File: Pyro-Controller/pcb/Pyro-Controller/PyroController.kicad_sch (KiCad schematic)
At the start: 8 parts, among them Q1 SiS454DN

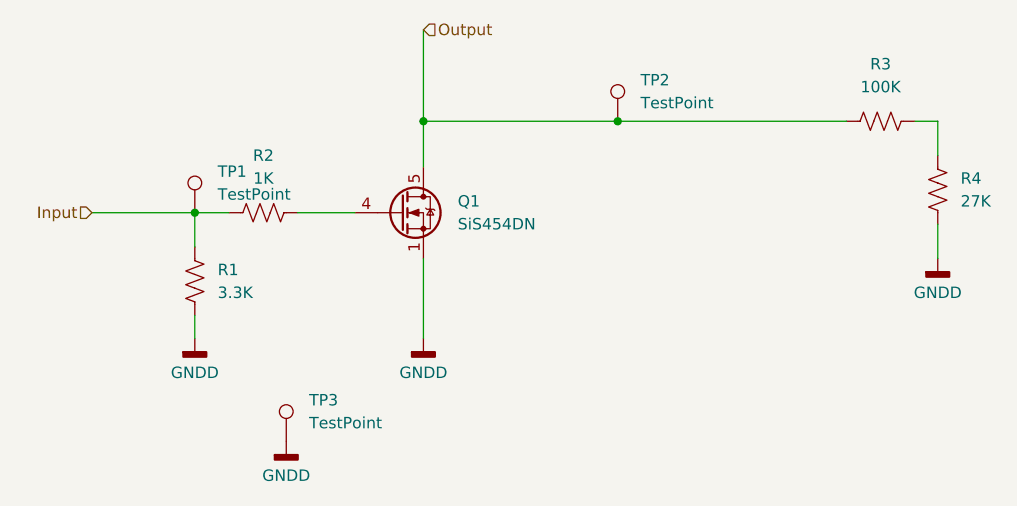
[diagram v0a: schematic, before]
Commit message: BOM, BOM Template, Rowan Rocketry Logo
- Finished pyro controller BOM
- Created template for BOMs
- Created a footprint for adding the Rowan Rocketry logo to PCBs
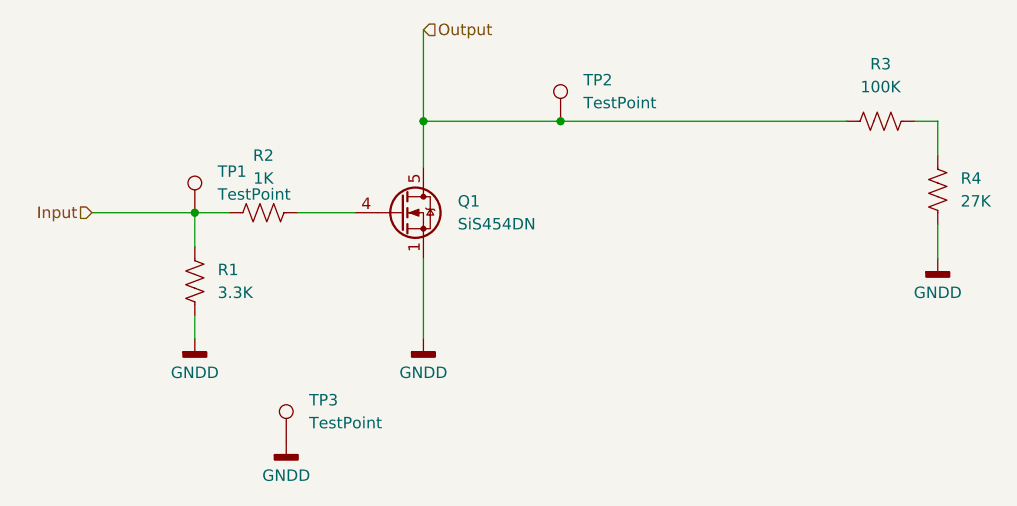
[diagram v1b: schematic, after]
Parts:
- Q1: Purchase (none) -> https://www.digikey.com/en/products/detail/vishay-siliconix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
- R1, R2, R4: Purchase (none) -> https://www.digikey.com/en/products/detail/yageo/RC0603JR-0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
- R3: Purchase (none) -> https://www.digikey.com/en/products/detail/yageo/RC0603JR-1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
- TP1, TP2, TP3: Purchase (none) -> https://www.digikey.com/en/products/detail/keystone-electro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
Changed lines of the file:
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@@
 	)
 	(junction
-		(at 137.16 77.47)
+		(at 130.81 77.47)
 		(diameter 0)
 		(color 0 0 0 0)
@@
 	(wire
 		(pts
-			(xy 137.16 77.47) (xy 162.56 77.47)
-		)
-		(stroke
-			(width 0)
-			(type default)
-		)
-	)
-	(wire
-		(pts
-			(xy 115.57 77.47) (xy 137.16 77.47)
+			(xy 115.57 77.47) (xy 130.81 77.47)
 		)
 		(stroke
@@
 		(pts
 			(xy 101.6 87.63) (xy 107.95 87.63)
+		)
+		(stroke
+			(width 0)
+			(type default)
+		)
+	)
+	(wire
+		(pts
+			(xy 130.81 77.47) (xy 162.56 77.47)
 		)
 		(stroke
@@
 			)
 		)
-		(property "Datasheet" "~"
+		(property "Datasheet" "https://www.yageo.com/upload/media/product/products/datasheet/rchip/PYu-RC_Group_51_RoHS_L_12.pdf"
 			(at 90.17 95.25 0)
 			(effects
@@
 			)
 		)
-		(property "MPN" ""
-			(at 90.17 95.25 0)
-			(effects
-				(font
-					(size 1.27 1.27)
-				)
-				(hide yes)
-			)
-		)
-		(property "Retailer" ""
+		(property "Purchase" "https://www.digikey.com/en/products/detail/yageo/RC0603JR-073K3L/726757?_gl=1*oprbzy*_up*MQ..&gclid=Cj0KCQjwj4K5BhDYARIsAD1Ly2qquIi0HITcnSJzEILMOtvyCB9wPLUQOH5qAcVxd7LGVxbBaQts_tIaAkVREALw_wcB"
 			(at 90.17 95.25 0)
 			(effects
@@
 			)
 		)
-		(property "Datasheet" "~"
+		(property "Datasheet" "https://www.yageo.com/upload/media/product/products/datasheet/rchip/PYu-RC_Group_51_RoHS_L_12.pdf"
 			(at 172.72 85.09 0)
 			(effects
@@
 			)
 		)
-		(property "MPN" ""
-			(at 172.72 85.09 0)
-			(effects
-				(font
-					(size 1.27 1.27)
-				)
-				(hide yes)
-			)
-		)
-		(property "Retailer" ""
+		(property "Purchase" "https://www.digikey.com/en/products/detail/yageo/RC0603JR-0727KL/726752"
 			(at 172.72 85.09 0)
 			(effects
@@
 			)
 		)
-		(property "Datasheet" "~"
+		(property "Datasheet" "https://www.yageo.com/upload/media/product/products/datasheet/rchip/PYu-RC_Group_51_RoHS_L_12.pdf"
 			(at 97.79 87.63 0)
 			(effects
@@
 			)
 		)
-		(property "MPN" ""
-			(at 97.79 87.63 0)
-			(effects
-				(font
-					(size 1.27 1.27)
-				)
-				(hide yes)
-			)
-		)
-		(property "Retailer" ""
+		(property "Purchase" "https://www.digikey.com/en/products/detail/yageo/RC0603JR-071KL/726677?_gl=1*1an2o6r*_up*MQ..&gclid=Cj0KCQjwj4K5BhDYARIsAD1Ly2qquIi0HITcnSJzEILMOtvyCB9wPLUQOH5qAcVxd7LGVxbBaQts_tIaAkVREALw_wcB"
 			(at 97.79 87.63 0)
 			(effects
@@
 	)
 	(symbol
+		(lib_id "Connector:TestPoint")
+		(at 130.81 77.47 0)
+		(unit 1)
+		(exclude_from_sim no)
+		(in_bom yes)
+		(on_board yes)
+		(dnp no)
+		(fields_autoplaced yes)
+		(property "Reference" "TP2"
+			(at 133.35 72.8979 0)
+			(effects
+				(font
+					(size 1.27 1.27)
+				)
+				(justify left)
+			)
+		)
+		(property "Value" "TestPoint"
+			(at 133.35 75.4379 0)
+			(effects
+				(font
+					(size 1.27 1.27)
+				)
+				(justify left)
+			)
+		)
+		(property "Footprint" "TestPoint:TestPoint_Loop_D2.54mm_Drill1.5mm_Beaded"
+			(at 135.89 77.47 0)
+			(effects
+				(font
+					(size 1.27 1.27)
+				)
+				(hide yes)
+			)
+		)
+		(property "Datasheet" "https://www.keyelco.com/userAssets/file/M65p56.pdf"
+			(at 135.89 77.47 0)
+			(effects
+				(font
+					(size 1.27 1.27)
+				)
+				(hide yes)
+			)
+		)
+		(property "Description" "test point"
+			(at 130.81 77.47 0)
+			(effects
+				(font
+					(size 1.27 1.27)
+				)
+				(hide yes)
+			)
+		)
+		(property "Purchase" "https://www.digikey.com/en/products/detail/keystone-electronics/5000/255326"
+			(at 130.81 77.47 0)
+			(effects
+				(font
+					(size 1.27 1.27)
+				)
+				(hide yes)
+			)
+		)
+		(pin "1"
+		)
+		(instances
+			(project "Pyro-Controller"
+				(path "/3d6591d1-15d3-4f90-b463-ad4ce370627d/d3fae8d6-dc5c-4ad1-8056-ef8170011280"
+					(reference "TP2")
+					(unit 1)
+				)
+			)
+		)
+	)
+	(symbol
 		(lib_id "Device:R_US")
 		(at 166.37 77.47 90)
@@
 			)
 		)
-		(property "Datasheet" "~"
+		(property "Datasheet" "https://www.yageo.com/upload/media/product/products/datasheet/rchip/PYu-RC_Group_51_RoHS_L_12.pdf"
 			(at 166.37 77.47 0)
 			(effects
@@
 			)
 		)
-		(property "MPN" ""
-			(at 166.37 77.47 0)
-			(effects
-				(font
-					(size 1.27 1.27)
-				)
-				(hide yes)
-			)
-		)
-		(property "Retailer" ""
+		(property "Purchase" "https://www.digikey.com/en/products/detail/yageo/RC0603JR-13100KL/13694230?_gl=1*1eq4xmo*_up*MQ..&gclid=Cj0KCQjwj4K5BhDYARIsAD1Ly2qquIi0HITcnSJzEILMOtvyCB9wPLUQOH5qAcVxd7LGVxbBaQts_tIaAkVREALw_wcB"
 			(at 166.37 77.47 0)
 			(effects
@@
 	(symbol
 		(lib_id "Connector:TestPoint")
-		(at 137.16 77.47 0)
-		(unit 1)
-		(exclude_from_sim no)
-		(in_bom yes)
-		(on_board yes)
-		(dnp no)
-		(fields_autoplaced yes)
-		(property "Reference" "TP2"
-			(at 139.7 72.8979 0)
+		(at 100.33 113.03 0)
+		(unit 1)
+		(exclude_from_sim no)
+		(in_bom yes)
+		(on_board yes)
+		(dnp no)
+		(fields_autoplaced yes)
+		(property "Reference" "TP3"
+			(at 102.87 108.4579 0)
 			(effects
 				(font
@@
 		)
 		(property "Value" "TestPoint"
-			(at 139.7 75.4379 0)
+			(at 102.87 110.9979 0)
 			(effects
 				(font
@@
 		)
 		(property "Footprint" "TestPoint:TestPoint_Loop_D2.54mm_Drill1.5mm_Beaded"
-			(at 142.24 77.47 0)
-			(effects
-				(font
-					(size 1.27 1.27)
-				)
-				(hide yes)
-			)
-		)
-		(property "Datasheet" "~"
-			(at 142.24 77.47 0)
+			(at 105.41 113.03 0)
+			(effects
+				(font
+					(size 1.27 1.27)
+				)
+				(hide yes)
+			)
+		)
+		(property "Datasheet" "https://www.keyelco.com/userAssets/file/M65p56.pdf"
+			(at 105.41 113.03 0)
 			(effects
 				(font
@@
 		)
 		(property "Description" "test point"
-			(at 137.16 77.47 0)
-			(effects
-				(font
-					(size 1.27 1.27)
-				)
-				(hide yes)
-			)
-		)
-		(property "MPN" ""
-			(at 137.16 77.47 0)
-			(effects
-				(font
-					(size 1.27 1.27)
-				)
-				(hide yes)
-			)
-		)
-		(property "Retailer" ""
-			(at 137.16 77.47 0)
+			(at 100.33 113.03 0)
+			(effects
+				(font
+					(size 1.27 1.27)
+				)
+				(hide yes)
+			)
+		)
+		(property "Purchase" "https://www.digikey.com/en/products/detail/keystone-electronics/5000/255326"
+			(at 100.33 113.03 0)
 			(effects
 				(font
@@
 			(project "Pyro-Controller"
 				(path "/3d6591d1-15d3-4f90-b463-ad4ce370627d/d3fae8d6-dc5c-4ad1-8056-ef8170011280"
-					(reference "TP2")
+					(reference "TP3")
 					(unit 1)
 				)
@@
 			)
 		)
-		(property "Datasheet" "~"
+		(property "Datasheet" "https://www.keyelco.com/userAssets/file/M65p56.pdf"
 			(at 95.25 87.63 0)
 			(effects
@@
 			)
 		)
-		(property "MPN" ""
-			(at 90.17 87.63 0)
-			(effects
-				(font
-					(size 1.27 1.27)
-				)
-				(hide yes)
-			)
-		)
-		(property "Retailer" ""
+		(property "Purchase" "https://www.digikey.com/en/products/detail/keystone-electronics/5000/255326"
 			(at 90.17 87.63 0)
 			(effects
@@
 	)
 	(symbol
-		(lib_id "Connector:TestPoint")
-		(at 100.33 113.03 0)
-		(unit 1)
-		(exclude_from_sim no)
-		(in_bom yes)
-		(on_board yes)
-		(dnp no)
-		(fields_autoplaced yes)
-		(property "Reference" "TP3"
-			(at 102.87 108.4579 0)
-			(effects
-				(font
-					(size 1.27 1.27)
-				)
-				(justify left)
-			)
-		)
-		(property "Value" "TestPoint"
-			(at 102.87 110.9979 0)
-			(effects
-				(font
-					(size 1.27 1.27)
-				)
-				(justify left)
-			)
-		)
-		(property "Footprint" "TestPoint:TestPoint_Loop_D2.54mm_Drill1.5mm_Beaded"
-			(at 105.41 113.03 0)
-			(effects
-				(font
-					(size 1.27 1.27)
-				)
-				(hide yes)
-			)
-		)
-		(property "Datasheet" "~"
-			(at 105.41 113.03 0)
-			(effects
-				(font
-					(size 1.27 1.27)
-				)
-				(hide yes)
-			)
-		)
-		(property "Description" "test point"
-			(at 100.33 113.03 0)
-			(effects
-				(font
-					(size 1.27 1.27)
-				)
-				(hide yes)
-			)
-		)
-		(property "MPN" ""
-			(at 100.33 113.03 0)
-			(effects
-				(font
-					(size 1.27 1.27)
-				)
-				(hide yes)
-			)
-		)
-		(property "Retailer" ""
-			(at 100.33 113.03 0)
-			(effects
-				(font
-					(size 1.27 1.27)
-				)
-				(hide yes)
-			)
-		)
-		(pin "1"
-		)
-		(instances
-			(project "Pyro-Controller"
-				(path "/3d6591d1-15d3-4f90-b463-ad4ce370627d/d3fae8d6-dc5c-4ad1-8056-ef8170011280"
-					(reference "TP3")
-					(unit 1)
-				)
-			)
-		)
-	)
-	(symbol
 		(lib_id "Transistor_FET:SiS454DN")
 		(at 113.03 87.63 0)
@@
 			)
 		)
-		(property "MPN" ""
+		(property "Purchase" "https://www.digikey.com/en/products/detail/vishay-siliconix/SIS454DN-T1-GE3/2441826?s=N4IgTCBcDaIMoEs4BYCsyAiA5EBdAvkA"
 			(at 113.03 87.63 0)
 			(effects
-				(font
-					(size 1.27 1.27)
-				)
-				(hide yes)
-			)
-		)
-		(property "Retailer" ""
-			(at 113.03 87.63 0)
-			(effects
